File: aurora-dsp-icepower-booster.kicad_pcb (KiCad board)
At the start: 2 copper layers, 0 parts

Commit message: chore: 🔄 update code structure for better maintainability
* Refactored multiple code sections to improve readability.
* Removed redundant code blocks to streamline functionality.
* Enhanced modularity for easier future updates.
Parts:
- added MH1: MountingHole_3.2mm, , F.Cu at (5.00, 5.00)
- added MH1: MountingHole, MountingHole:MountingHole_3.2mm_M3_Pad, F.Cu at (5.00, 5.00)
- added MH2: MountingHole, MountingHole:MountingHole_3.2mm_M3_Pad, F.Cu at (195.0, 5.00)
- added MH3: MountingHole, MountingHole:MountingHole_3.2mm_M3_Pad, F.Cu at (5.00, 165.0)
- added MH4: MountingHole, MountingHole:MountingHole_3.2mm_M3_Pad, F.Cu at (195.0, 165.0)
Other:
- board outline added: 200 x 170 mm

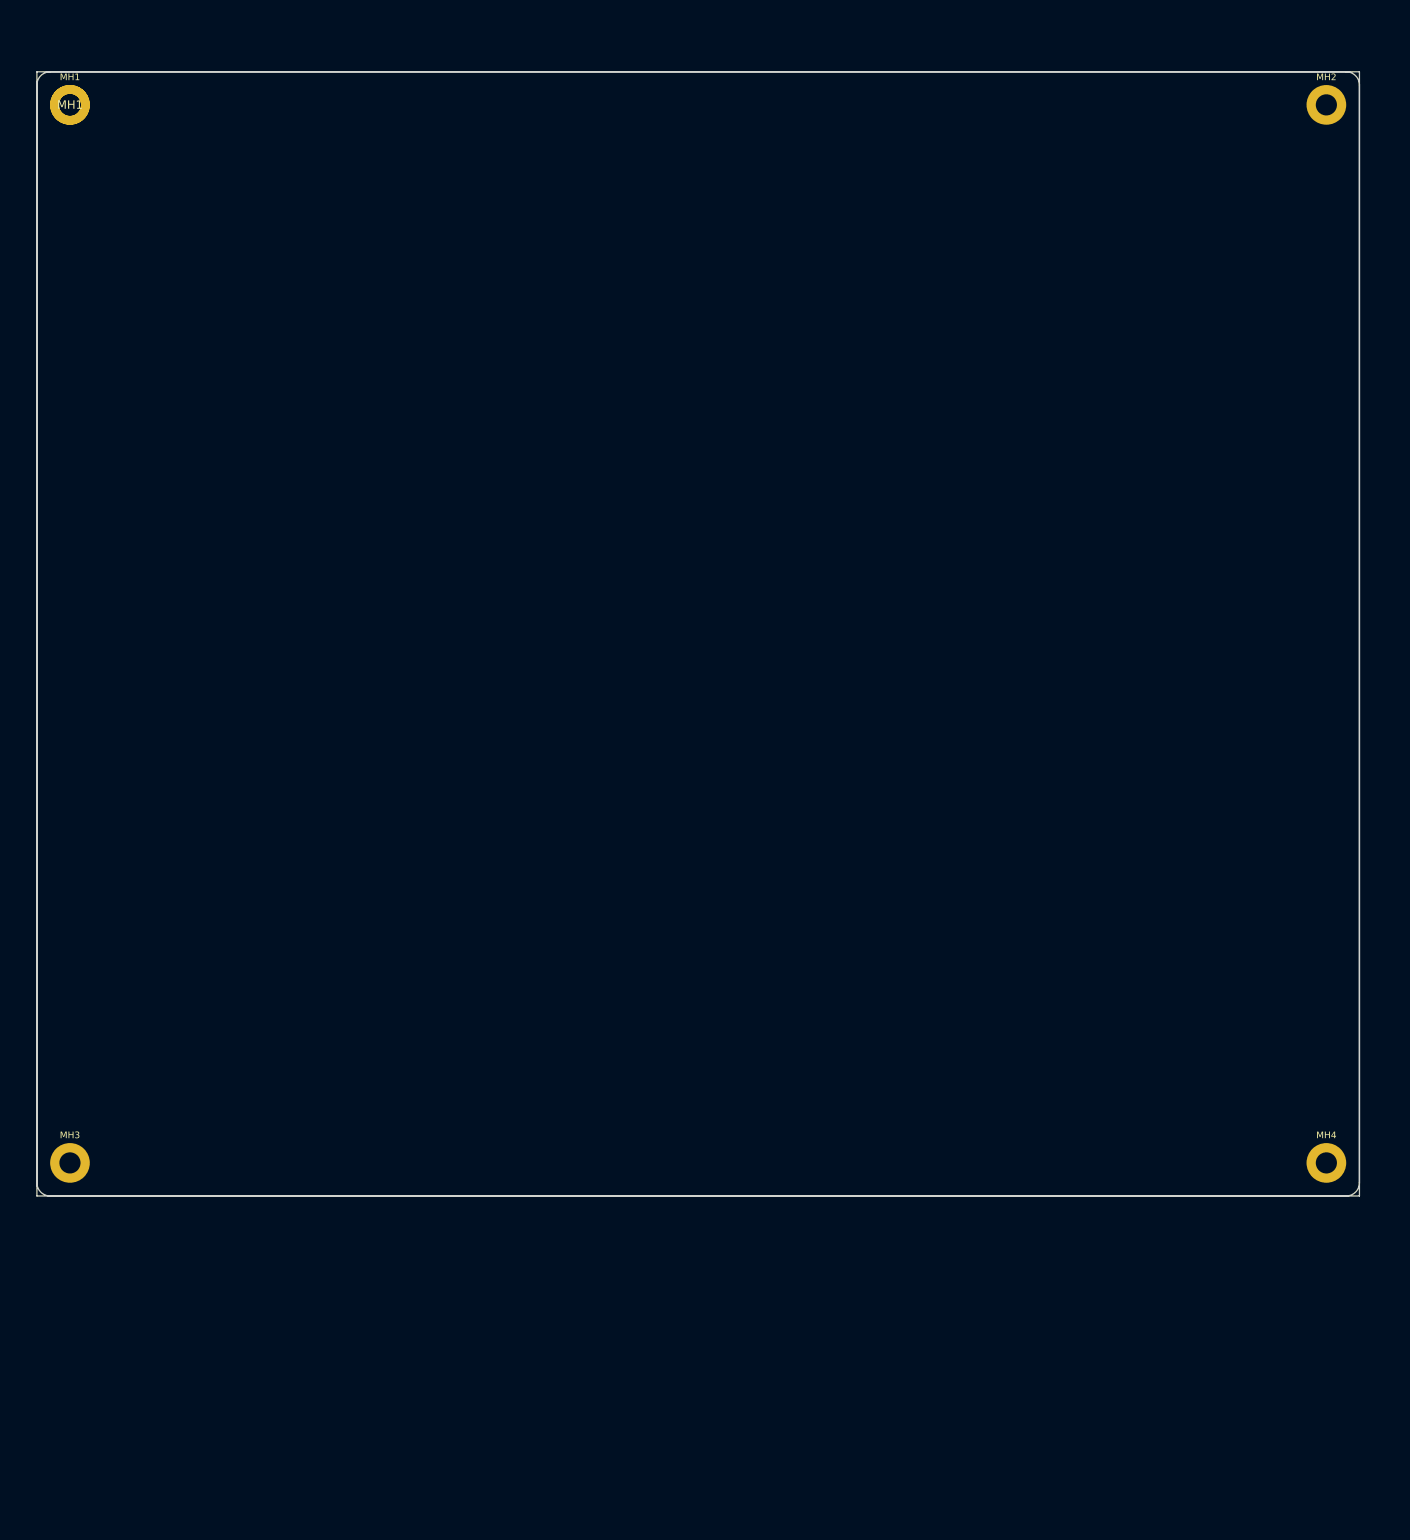
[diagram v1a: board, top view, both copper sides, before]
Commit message: feat: PCB layout v8 — routing 67%, cleanup & documentation
Schematic: 264 symbols, 0 ERC errors, all annotated
PCB: 243 footprints, 200x200mm 2-layer, v8 routing (271/400, 67%)
- Phase 0-3 complete (sync, board setup, placement)
- Phase 4 routing v8: A* pathfinding, 144 GND vias, GND zone B.Cu
- DRC: 269 violations (18 shorts, WIP), 399 unconnected (WIP)

Added:
- .gitignore for KiCad project
- FINDINGS.md: quality gate & circuit analysis
- datasheets/: ICEpower module datasheets, research docs
- scripts/pcb/: placement, netclass, mounting hole scripts
- scripts/reformat_sch.py, replicate_channels.py
- .github/skills/kicad-schematic/: references & validation scripts

Cleanup:
- Removed 13 .bak files, backups/ directory
- Removed 219 temp scripts from /tmp
- Updated .gitignore to cover *.bak*, ERC/DRC JSON, OS files
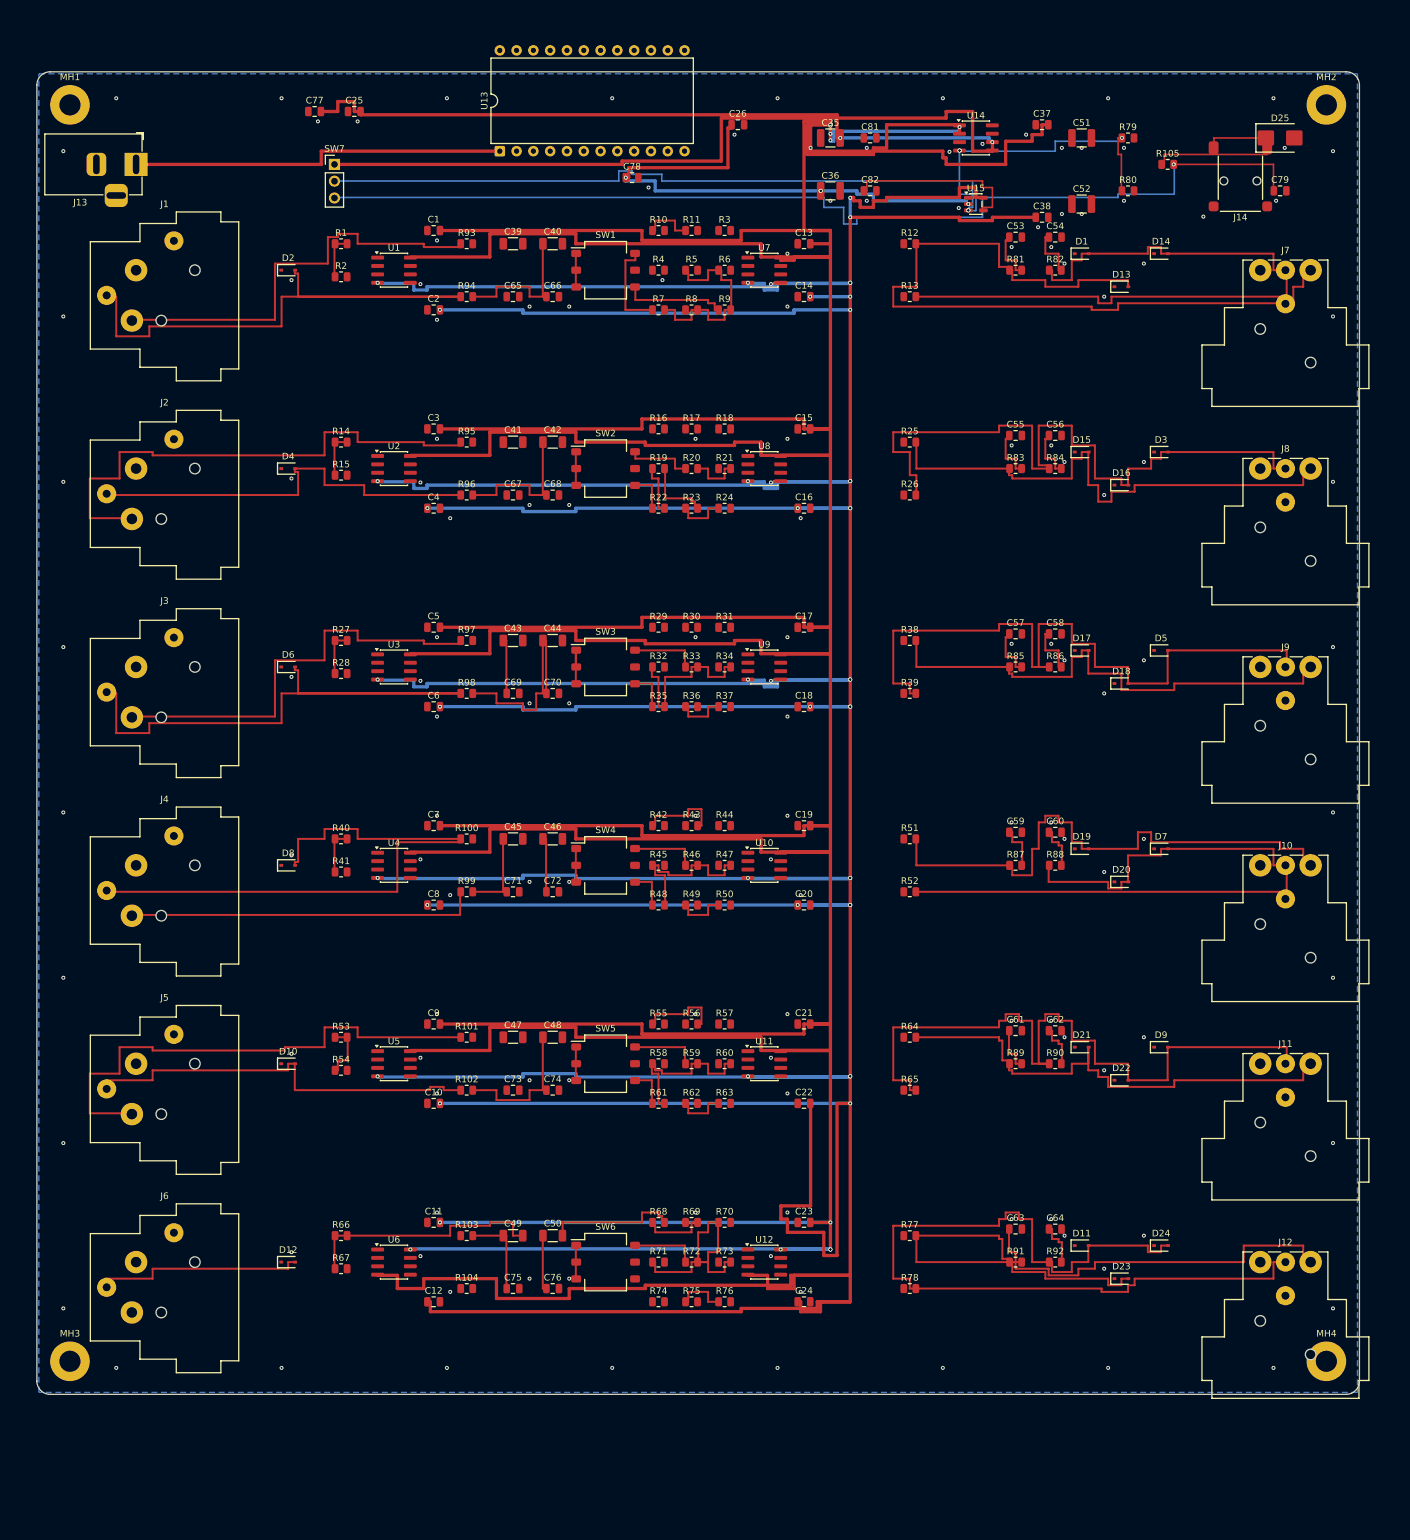
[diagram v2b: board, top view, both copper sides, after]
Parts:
- removed the MH1 at (5.00, 5.00)
- added C1: 100nF C0G, Capacitor_SMD:C_0805_2012Metric, F.Cu at (60.0, 24.0)
- added C10: 100nF C0G, Capacitor_SMD:C_0805_2012Metric, F.Cu at (60.0, 156.0)
- added C11: 100nF C0G, Capacitor_SMD:C_0805_2012Metric, F.Cu at (60.0, 174.0)
- added C12: 100nF C0G, Capacitor_SMD:C_0805_2012Metric, F.Cu at (60.0, 186.0)
- added C13: 100nF C0G, Capacitor_SMD:C_0805_2012Metric, F.Cu at (116.0, 26.0)
- added C14: 100nF C0G, Capacitor_SMD:C_0805_2012Metric, F.Cu at (116.0, 34.0)
- added C15: 100nF C0G, Capacitor_SMD:C_0805_2012Metric, F.Cu at (116.0, 54.0)
- added C16: 100nF C0G, Capacitor_SMD:C_0805_2012Metric, F.Cu at (116.0, 66.0)
- added C17: 100nF C0G, Capacitor_SMD:C_0805_2012Metric, F.Cu at (116.0, 84.0)
- added C18: 100nF C0G, Capacitor_SMD:C_0805_2012Metric, F.Cu at (116.0, 96.0)
- added C19: 100nF C0G, Capacitor_SMD:C_0805_2012Metric, F.Cu at (116.0, 114.0)
- added C2: 100nF C0G, Capacitor_SMD:C_0805_2012Metric, F.Cu at (60.0, 36.0)
- added C20: 100nF C0G, Capacitor_SMD:C_0805_2012Metric, F.Cu at (116.0, 126.0)
- added C21: 100nF C0G, Capacitor_SMD:C_0805_2012Metric, F.Cu at (116.0, 144.0)
- added C22: 100nF C0G, Capacitor_SMD:C_0805_2012Metric, F.Cu at (116.0, 156.0)
- added C23: 100nF C0G, Capacitor_SMD:C_0805_2012Metric, F.Cu at (116.0, 174.0)
- added C24: 100nF C0G, Capacitor_SMD:C_0805_2012Metric, F.Cu at (116.0, 186.0)
- added C25: 100nF C0G, Capacitor_SMD:C_0805_2012Metric, F.Cu at (48.0, 6.00)
- added C26: 100nF C0G, Capacitor_SMD:C_0805_2012Metric, F.Cu at (106.0, 8.00)
- added C3: 100nF C0G, Capacitor_SMD:C_0805_2012Metric, F.Cu at (60.0, 54.0)
- added C35: 100uF/25V, Capacitor_SMD:C_1210_3225Metric, F.Cu at (120.0, 10.0)
- added C36: 100uF/25V, Capacitor_SMD:C_1210_3225Metric, F.Cu at (120.0, 18.0)
- added C37: 10uF X5R, Capacitor_SMD:C_0805_2012Metric, F.Cu at (152.0, 8.00)
- added C38: 10uF X5R, Capacitor_SMD:C_0805_2012Metric, F.Cu at (152.0, 22.0)
- added C39: 2.2uF C0G, Capacitor_SMD:C_1206_3216Metric, F.Cu at (72.0, 26.0)
- added C4: 100nF C0G, Capacitor_SMD:C_0805_2012Metric, F.Cu at (60.0, 66.0)
- added C40: 2.2uF C0G, Capacitor_SMD:C_1206_3216Metric, F.Cu at (78.0, 26.0)
- added C41: 2.2uF C0G, Capacitor_SMD:C_1206_3216Metric, F.Cu at (72.0, 56.0)
- added C42: 2.2uF C0G, Capacitor_SMD:C_1206_3216Metric, F.Cu at (78.0, 56.0)
- added C43: 2.2uF C0G, Capacitor_SMD:C_1206_3216Metric, F.Cu at (72.0, 86.0)
- added C44: 2.2uF C0G, Capacitor_SMD:C_1206_3216Metric, F.Cu at (78.0, 86.0)
- added C45: 2.2uF C0G, Capacitor_SMD:C_1206_3216Metric, F.Cu at (72.0, 116.0)
- added C46: 2.2uF C0G, Capacitor_SMD:C_1206_3216Metric, F.Cu at (78.0, 116.0)
- added C47: 2.2uF C0G, Capacitor_SMD:C_1206_3216Metric, F.Cu at (72.0, 146.0)
- added C48: 2.2uF C0G, Capacitor_SMD:C_1206_3216Metric, F.Cu at (78.0, 146.0)
- added C49: 2.2uF C0G, Capacitor_SMD:C_1206_3216Metric, F.Cu at (72.0, 176.0)
- added C5: 100nF C0G, Capacitor_SMD:C_0805_2012Metric, F.Cu at (60.0, 84.0)
- added C50: 2.2uF C0G, Capacitor_SMD:C_1206_3216Metric, F.Cu at (78.0, 176.0)
- added C51: 100uF, Capacitor_SMD:C_1210_3225Metric, F.Cu at (158.0, 10.0)
- added C52: 100uF, Capacitor_SMD:C_1210_3225Metric, F.Cu at (158.0, 20.0)
- added C53: 100nF C0G, Capacitor_SMD:C_0805_2012Metric, F.Cu at (148.0, 25.0)
- added C54: 100nF C0G, Capacitor_SMD:C_0805_2012Metric, F.Cu at (154.0, 25.0)
- added C55: 100nF C0G, Capacitor_SMD:C_0805_2012Metric, F.Cu at (148.0, 55.0)
- added C56: 100nF C0G, Capacitor_SMD:C_0805_2012Metric, F.Cu at (154.0, 55.0)
- added C57: 100nF C0G, Capacitor_SMD:C_0805_2012Metric, F.Cu at (148.0, 85.0)
- added C58: 100nF C0G, Capacitor_SMD:C_0805_2012Metric, F.Cu at (154.0, 85.0)
- added C59: 100nF C0G, Capacitor_SMD:C_0805_2012Metric, F.Cu at (148.0, 115.0)
- added C6: 100nF C0G, Capacitor_SMD:C_0805_2012Metric, F.Cu at (60.0, 96.0)
- added C60: 100nF C0G, Capacitor_SMD:C_0805_2012Metric, F.Cu at (154.0, 115.0)
- added C61: 100nF C0G, Capacitor_SMD:C_0805_2012Metric, F.Cu at (148.0, 145.0)
- added C62: 100nF C0G, Capacitor_SMD:C_0805_2012Metric, F.Cu at (154.0, 145.0)
- added C63: 100nF C0G, Capacitor_SMD:C_0805_2012Metric, F.Cu at (148.0, 175.0)
- added C64: 100nF C0G, Capacitor_SMD:C_0805_2012Metric, F.Cu at (154.0, 175.0)
- added C65: 100pF C0G, Capacitor_SMD:C_0805_2012Metric, F.Cu at (72.0, 34.0)
- added C66: 100pF C0G, Capacitor_SMD:C_0805_2012Metric, F.Cu at (78.0, 34.0)
- added C67: 100pF C0G, Capacitor_SMD:C_0805_2012Metric, F.Cu at (72.0, 64.0)
- added C68: 100pF C0G, Capacitor_SMD:C_0805_2012Metric, F.Cu at (78.0, 64.0)
- added C69: 100pF C0G, Capacitor_SMD:C_0805_2012Metric, F.Cu at (72.0, 94.0)
- added C7: 100nF C0G, Capacitor_SMD:C_0805_2012Metric, F.Cu at (60.0, 114.0)
- added C70: 100pF C0G, Capacitor_SMD:C_0805_2012Metric, F.Cu at (78.0, 94.0)
- added C71: 100pF C0G, Capacitor_SMD:C_0805_2012Metric, F.Cu at (72.0, 124.0)
- added C72: 100pF C0G, Capacitor_SMD:C_0805_2012Metric, F.Cu at (78.0, 124.0)
- added C73: 100pF C0G, Capacitor_SMD:C_0805_2012Metric, F.Cu at (72.0, 154.0)
- added C74: 100pF C0G, Capacitor_SMD:C_0805_2012Metric, F.Cu at (78.0, 154.0)
- added C75: 100pF C0G, Capacitor_SMD:C_0805_2012Metric, F.Cu at (72.0, 184.0)
- added C76: 100pF C0G, Capacitor_SMD:C_0805_2012Metric, F.Cu at (78.0, 184.0)
- added C77: 100nF C0G, Capacitor_SMD:C_0805_2012Metric, F.Cu at (42.0, 6.00)
- added C78: 100nF C0G, Capacitor_SMD:C_0805_2012Metric, F.Cu at (90.0, 16.0)
- added C79: 100nF C0G, Capacitor_SMD:C_0805_2012Metric, F.Cu at (188.0, 18.0)
- added C8: 100nF C0G, Capacitor_SMD:C_0805_2012Metric, F.Cu at (60.0, 126.0)
- added C81: 100nF C0G, Capacitor_SMD:C_0805_2012Metric, F.Cu at (126.0, 10.0)
- added C82: 100nF C0G, Capacitor_SMD:C_0805_2012Metric, F.Cu at (126.0, 18.0)
- added C9: 100nF C0G, Capacitor_SMD:C_0805_2012Metric, F.Cu at (60.0, 144.0)
- added D1: PESD5V0S1BL, Diode_SMD:D_SOD-323, F.Cu at (158.0, 27.5)
- added D10: PESD5V0S1BL, Diode_SMD:D_SOD-323, F.Cu at (38.0, 150.0)
- added D11: PESD5V0S1BL, Diode_SMD:D_SOD-323, F.Cu at (158.0, 177.5)
- added D12: PESD5V0S1BL, Diode_SMD:D_SOD-323, F.Cu at (38.0, 180.0)
- added D13: PESD5V0S1BL, Diode_SMD:D_SOD-323, F.Cu at (164.0, 32.5)
- added D14: PESD5V0S1BL, Diode_SMD:D_SOD-323, F.Cu at (170.0, 27.5)
- added D15: PESD5V0S1BL, Diode_SMD:D_SOD-323, F.Cu at (158.0, 57.5)
- added D16: PESD5V0S1BL, Diode_SMD:D_SOD-323, F.Cu at (164.0, 62.5)
- added D17: PESD5V0S1BL, Diode_SMD:D_SOD-323, F.Cu at (158.0, 87.5)
- added D18: PESD5V0S1BL, Diode_SMD:D_SOD-323, F.Cu at (164.0, 92.5)
- added D19: PESD5V0S1BL, Diode_SMD:D_SOD-323, F.Cu at (158.0, 117.5)
- added D2: PESD5V0S1BL, Diode_SMD:D_SOD-323, F.Cu at (38.0, 30.0)
- added D20: PESD5V0S1BL, Diode_SMD:D_SOD-323, F.Cu at (164.0, 122.5)
- added D21: PESD5V0S1BL, Diode_SMD:D_SOD-323, F.Cu at (158.0, 147.5)
- added D22: PESD5V0S1BL, Diode_SMD:D_SOD-323, F.Cu at (164.0, 152.5)
- added D23: PESD5V0S1BL, Diode_SMD:D_SOD-323, F.Cu at (164.0, 182.5)
- added D24: PESD5V0S1BL, Diode_SMD:D_SOD-323, F.Cu at (170.0, 177.5)
- added D25: SMBJ15CA, Diode_SMD:D_SMB, F.Cu at (188.0, 10.0)
- added D3: PESD5V0S1BL, Diode_SMD:D_SOD-323, F.Cu at (170.0, 57.5)
- added D4: PESD5V0S1BL, Diode_SMD:D_SOD-323, F.Cu at (38.0, 60.0)
- added D5: PESD5V0S1BL, Diode_SMD:D_SOD-323, F.Cu at (170.0, 87.5)
- added D6: PESD5V0S1BL, Diode_SMD:D_SOD-323, F.Cu at (38.0, 90.0)
- added D7: PESD5V0S1BL, Diode_SMD:D_SOD-323, F.Cu at (170.0, 117.5)
- added D8: PESD5V0S1BL, Diode_SMD:D_SOD-323, F.Cu at (38.0, 120.0)
- added D9: PESD5V0S1BL, Diode_SMD:D_SOD-323, F.Cu at (170.0, 147.5)
- added J1: XLR_IN_1, Connector_Audio:Jack_XLR_Neutrik_NC3FBH2_Horizontal, F.Cu at (15.0, 30.0)
- added J10: XLR3_OUT, Connector_Audio:Jack_XLR_Neutrik_NC3MBH_Horizontal, F.Cu at (185.0, 120.0)
- added J11: XLR3_OUT, Connector_Audio:Jack_XLR_Neutrik_NC3MBH_Horizontal, F.Cu at (185.0, 150.0)
- added J12: XLR3_OUT, Connector_Audio:Jack_XLR_Neutrik_NC3MBH_Horizontal, F.Cu at (185.0, 180.0)
- added J13: 24V DC, Connector_BarrelJack:BarrelJack_Horizontal, F.Cu at (15.0, 14.0)
- added J14: REMOTE 3.5mm, Connector_Audio:Jack_3.5mm_Lumberg_1503_02_Horizontal, F.Cu at (182.0, 14.0)
- added J2: XLR_IN_2, Connector_Audio:Jack_XLR_Neutrik_NC3FBH2_Horizontal, F.Cu at (15.0, 60.0)
- added J3: XLR_IN_3, Connector_Audio:Jack_XLR_Neutrik_NC3FBH2_Horizontal, F.Cu at (15.0, 90.0)
- added J4: XLR_IN_4, Connector_Audio:Jack_XLR_Neutrik_NC3FBH2_Horizontal, F.Cu at (15.0, 120.0)
- added J5: XLR_IN_5, Connector_Audio:Jack_XLR_Neutrik_NC3FBH2_Horizontal, F.Cu at (15.0, 150.0)
- added J6: XLR_IN_6, Connector_Audio:Jack_XLR_Neutrik_NC3FBH2_Horizontal, F.Cu at (15.0, 180.0)
- added J7: XLR3_OUT, Connector_Audio:Jack_XLR_Neutrik_NC3MBH_Horizontal, F.Cu at (185.0, 30.0)
- added J8: XLR3_OUT, Connector_Audio:Jack_XLR_Neutrik_NC3MBH_Horizontal, F.Cu at (185.0, 60.0)
- added J9: XLR3_OUT, Connector_Audio:Jack_XLR_Neutrik_NC3MBH_Horizontal, F.Cu at (185.0, 90.0)
- added R1: 10k 0.1%, Resistor_SMD:R_0805_2012Metric, F.Cu at (46.0, 26.0)
- added R10: 10k, Resistor_SMD:R_0805_2012Metric, F.Cu at (94.0, 24.0)
- added R100: 47, Resistor_SMD:R_0805_2012Metric, F.Cu at (65.0, 116.0)
- added R101: 47, Resistor_SMD:R_0805_2012Metric, F.Cu at (65.0, 146.0)
- added R102: 47, Resistor_SMD:R_0805_2012Metric, F.Cu at (65.0, 154.0)
- added R103: 47, Resistor_SMD:R_0805_2012Metric, F.Cu at (65.0, 176.0)
- added R104: 47, Resistor_SMD:R_0805_2012Metric, F.Cu at (65.0, 184.0)
- added R105: 10k, Resistor_SMD:R_0805_2012Metric, F.Cu at (171.0, 14.0)
- added R11: 10k, Resistor_SMD:R_0805_2012Metric, F.Cu at (99.0, 24.0)
- added R12: 47, Resistor_SMD:R_0805_2012Metric, F.Cu at (132.0, 26.0)
- added R13: 47, Resistor_SMD:R_0805_2012Metric, F.Cu at (132.0, 34.0)
- added R14: 10k 0.1%, Resistor_SMD:R_0805_2012Metric, F.Cu at (46.0, 56.0)
- added R15: 10k 0.1%, Resistor_SMD:R_0805_2012Metric, F.Cu at (46.0, 61.0)
- added R16: 10k 0.1%, Resistor_SMD:R_0805_2012Metric, F.Cu at (94.0, 54.0)
- added R17: 10k 0.1%, Resistor_SMD:R_0805_2012Metric, F.Cu at (99.0, 54.0)
- added R18: 10k 0.1%, Resistor_SMD:R_0805_2012Metric, F.Cu at (104.0, 54.0)
- added R19: 10k 0.1%, Resistor_SMD:R_0805_2012Metric, F.Cu at (94.0, 60.0)
- added R2: 10k 0.1%, Resistor_SMD:R_0805_2012Metric, F.Cu at (46.0, 31.0)
- added R20: 30k, Resistor_SMD:R_0805_2012Metric, F.Cu at (99.0, 60.0)
- added R21: 15k, Resistor_SMD:R_0805_2012Metric, F.Cu at (104.0, 60.0)
- added R22: 7.5k, Resistor_SMD:R_0805_2012Metric, F.Cu at (94.0, 66.0)
- added R23: 10k, Resistor_SMD:R_0805_2012Metric, F.Cu at (99.0, 66.0)
- added R24: 10k, Resistor_SMD:R_0805_2012Metric, F.Cu at (104.0, 66.0)
- added R25: 47, Resistor_SMD:R_0805_2012Metric, F.Cu at (132.0, 56.0)
- added R26: 47, Resistor_SMD:R_0805_2012Metric, F.Cu at (132.0, 64.0)
- added R27: 10k 0.1%, Resistor_SMD:R_0805_2012Metric, F.Cu at (46.0, 86.0)
- added R28: 10k 0.1%, Resistor_SMD:R_0805_2012Metric, F.Cu at (46.0, 91.0)
- added R29: 10k 0.1%, Resistor_SMD:R_0805_2012Metric, F.Cu at (94.0, 84.0)
- added R3: 10k 0.1%, Resistor_SMD:R_0805_2012Metric, F.Cu at (104.0, 24.0)
- added R30: 10k 0.1%, Resistor_SMD:R_0805_2012Metric, F.Cu at (99.0, 84.0)
- added R31: 10k 0.1%, Resistor_SMD:R_0805_2012Metric, F.Cu at (104.0, 84.0)
- added R32: 10k 0.1%, Resistor_SMD:R_0805_2012Metric, F.Cu at (94.0, 90.0)
- added R33: 30k, Resistor_SMD:R_0805_2012Metric, F.Cu at (99.0, 90.0)
- added R34: 15k, Resistor_SMD:R_0805_2012Metric, F.Cu at (104.0, 90.0)
- added R35: 7.5k, Resistor_SMD:R_0805_2012Metric, F.Cu at (94.0, 96.0)
- added R36: 10k, Resistor_SMD:R_0805_2012Metric, F.Cu at (99.0, 96.0)
- added R37: 10k, Resistor_SMD:R_0805_2012Metric, F.Cu at (104.0, 96.0)
- added R38: 47, Resistor_SMD:R_0805_2012Metric, F.Cu at (132.0, 86.0)
- added R39: 47, Resistor_SMD:R_0805_2012Metric, F.Cu at (132.0, 94.0)
- added R4: 10k 0.1%, Resistor_SMD:R_0805_2012Metric, F.Cu at (94.0, 30.0)
- added R40: 10k 0.1%, Resistor_SMD:R_0805_2012Metric, F.Cu at (46.0, 116.0)
- added R41: 10k 0.1%, Resistor_SMD:R_0805_2012Metric, F.Cu at (46.0, 121.0)
- added R42: 10k 0.1%, Resistor_SMD:R_0805_2012Metric, F.Cu at (94.0, 114.0)
- added R43: 10k 0.1%, Resistor_SMD:R_0805_2012Metric, F.Cu at (99.0, 114.0)
- added R44: 10k 0.1%, Resistor_SMD:R_0805_2012Metric, F.Cu at (104.0, 114.0)
- added R45: 10k 0.1%, Resistor_SMD:R_0805_2012Metric, F.Cu at (94.0, 120.0)
- added R46: 30k, Resistor_SMD:R_0805_2012Metric, F.Cu at (99.0, 120.0)
- added R47: 15k, Resistor_SMD:R_0805_2012Metric, F.Cu at (104.0, 120.0)
- added R48: 7.5k, Resistor_SMD:R_0805_2012Metric, F.Cu at (94.0, 126.0)
- added R49: 10k, Resistor_SMD:R_0805_2012Metric, F.Cu at (99.0, 126.0)
- added R5: 10k 0.1%, Resistor_SMD:R_0805_2012Metric, F.Cu at (99.0, 30.0)
- added R50: 10k, Resistor_SMD:R_0805_2012Metric, F.Cu at (104.0, 126.0)
- added R51: 47, Resistor_SMD:R_0805_2012Metric, F.Cu at (132.0, 116.0)
- added R52: 47, Resistor_SMD:R_0805_2012Metric, F.Cu at (132.0, 124.0)
- added R53: 10k 0.1%, Resistor_SMD:R_0805_2012Metric, F.Cu at (46.0, 146.0)
- added R54: 10k 0.1%, Resistor_SMD:R_0805_2012Metric, F.Cu at (46.0, 151.0)
- added R55: 10k 0.1%, Resistor_SMD:R_0805_2012Metric, F.Cu at (94.0, 144.0)
- added R56: 10k 0.1%, Resistor_SMD:R_0805_2012Metric, F.Cu at (99.0, 144.0)
- added R57: 10k 0.1%, Resistor_SMD:R_0805_2012Metric, F.Cu at (104.0, 144.0)
- added R58: 10k 0.1%, Resistor_SMD:R_0805_2012Metric, F.Cu at (94.0, 150.0)
- added R59: 30k, Resistor_SMD:R_0805_2012Metric, F.Cu at (99.0, 150.0)
- added R6: 10k 0.1%, Resistor_SMD:R_0805_2012Metric, F.Cu at (104.0, 30.0)
- added R60: 15k, Resistor_SMD:R_0805_2012Metric, F.Cu at (104.0, 150.0)
- added R61: 7.5k, Resistor_SMD:R_0805_2012Metric, F.Cu at (94.0, 156.0)
- added R62: 10k, Resistor_SMD:R_0805_2012Metric, F.Cu at (99.0, 156.0)
- added R63: 10k, Resistor_SMD:R_0805_2012Metric, F.Cu at (104.0, 156.0)
- added R64: 47, Resistor_SMD:R_0805_2012Metric, F.Cu at (132.0, 146.0)
- added R65: 47, Resistor_SMD:R_0805_2012Metric, F.Cu at (132.0, 154.0)
- added R66: 10k 0.1%, Resistor_SMD:R_0805_2012Metric, F.Cu at (46.0, 176.0)
- added R67: 10k 0.1%, Resistor_SMD:R_0805_2012Metric, F.Cu at (46.0, 181.0)
- added R68: 10k 0.1%, Resistor_SMD:R_0805_2012Metric, F.Cu at (94.0, 174.0)
- added R69: 10k 0.1%, Resistor_SMD:R_0805_2012Metric, F.Cu at (99.0, 174.0)
- added R7: 30k, Resistor_SMD:R_0805_2012Metric, F.Cu at (94.0, 36.0)
- added R70: 10k 0.1%, Resistor_SMD:R_0805_2012Metric, F.Cu at (104.0, 174.0)
- added R71: 10k 0.1%, Resistor_SMD:R_0805_2012Metric, F.Cu at (94.0, 180.0)
- added R72: 30k, Resistor_SMD:R_0805_2012Metric, F.Cu at (99.0, 180.0)
- added R73: 15k, Resistor_SMD:R_0805_2012Metric, F.Cu at (104.0, 180.0)
- added R74: 7.5k, Resistor_SMD:R_0805_2012Metric, F.Cu at (94.0, 186.0)
- added R75: 10k, Resistor_SMD:R_0805_2012Metric, F.Cu at (99.0, 186.0)
- added R76: 10k, Resistor_SMD:R_0805_2012Metric, F.Cu at (104.0, 186.0)
- added R77: 47, Resistor_SMD:R_0805_2012Metric, F.Cu at (132.0, 176.0)
- added R78: 47, Resistor_SMD:R_0805_2012Metric, F.Cu at (132.0, 184.0)
- added R79: 100k, Resistor_SMD:R_0805_2012Metric, F.Cu at (165.0, 10.0)
- added R8: 15k, Resistor_SMD:R_0805_2012Metric, F.Cu at (99.0, 36.0)
- added R80: 100k, Resistor_SMD:R_0805_2012Metric, F.Cu at (165.0, 18.0)
- added R81: 10, Resistor_SMD:R_0805_2012Metric, F.Cu at (148.0, 30.0)
- added R82: 10, Resistor_SMD:R_0805_2012Metric, F.Cu at (154.0, 30.0)
- added R83: 10, Resistor_SMD:R_0805_2012Metric, F.Cu at (148.0, 60.0)
- added R84: 10, Resistor_SMD:R_0805_2012Metric, F.Cu at (154.0, 60.0)
- added R85: 10, Resistor_SMD:R_0805_2012Metric, F.Cu at (148.0, 90.0)
- added R86: 10, Resistor_SMD:R_0805_2012Metric, F.Cu at (154.0, 90.0)
- added R87: 10, Resistor_SMD:R_0805_2012Metric, F.Cu at (148.0, 120.0)
- added R88: 10, Resistor_SMD:R_0805_2012Metric, F.Cu at (154.0, 120.0)
- added R89: 10, Resistor_SMD:R_0805_2012Metric, F.Cu at (148.0, 150.0)
- added R9: 7.5k, Resistor_SMD:R_0805_2012Metric, F.Cu at (104.0, 36.0)
- added R90: 10, Resistor_SMD:R_0805_2012Metric, F.Cu at (154.0, 150.0)
- added R91: 10, Resistor_SMD:R_0805_2012Metric, F.Cu at (148.0, 180.0)
- added R92: 10, Resistor_SMD:R_0805_2012Metric, F.Cu at (154.0, 180.0)
- added R93: 47, Resistor_SMD:R_0805_2012Metric, F.Cu at (65.0, 26.0)
- added R94: 47, Resistor_SMD:R_0805_2012Metric, F.Cu at (65.0, 34.0)
- added R95: 47, Resistor_SMD:R_0805_2012Metric, F.Cu at (65.0, 56.0)
- added R96: 47, Resistor_SMD:R_0805_2012Metric, F.Cu at (65.0, 64.0)
- added R97: 47, Resistor_SMD:R_0805_2012Metric, F.Cu at (65.0, 86.0)
- added R98: 47, Resistor_SMD:R_0805_2012Metric, F.Cu at (65.0, 94.0)
- added R99: 47, Resistor_SMD:R_0805_2012Metric, F.Cu at (65.0, 124.0)
- added SW1: Gain CH1, Button_Switch_SMD:SW_DIP_SPSTx03_Slide_Omron_A6S-310x_W8.9mm_P2.54mm, F.Cu at (86.0, 30.0)
- added SW2: Gain CH2, Button_Switch_SMD:SW_DIP_SPSTx03_Slide_Omron_A6S-310x_W8.9mm_P2.54mm, F.Cu at (86.0, 60.0)
- added SW3: Gain CH3, Button_Switch_SMD:SW_DIP_SPSTx03_Slide_Omron_A6S-310x_W8.9mm_P2.54mm, F.Cu at (86.0, 90.0)
- added SW4: Gain CH4, Button_Switch_SMD:SW_DIP_SPSTx03_Slide_Omron_A6S-310x_W8.9mm_P2.54mm, F.Cu at (86.0, 120.0)
- added SW5: Gain CH5, Button_Switch_SMD:SW_DIP_SPSTx03_Slide_Omron_A6S-310x_W8.9mm_P2.54mm, F.Cu at (86.0, 150.0)
- added SW6: Gain CH6, Button_Switch_SMD:SW_DIP_SPSTx03_Slide_Omron_A6S-310x_W8.9mm_P2.54mm, F.Cu at (86.0, 180.0)
- added SW7: ALWAYS/REMOTE, Connector_PinHeader_2.54mm:PinHeader_1x03_P2.54mm_Vertical, F.Cu at (45.0, 14.0)
- added U1: LM4562, Package_SO:SOIC-8_3.9x4.9mm_P1.27mm, F.Cu at (54.0, 30.0)
- added U10: LM4562, Package_SO:SOIC-8_3.9x4.9mm_P1.27mm, F.Cu at (110.0, 120.0)
- added U11: LM4562, Package_SO:SOIC-8_3.9x4.9mm_P1.27mm, F.Cu at (110.0, 150.0)
- added U12: LM4562, Package_SO:SOIC-8_3.9x4.9mm_P1.27mm, F.Cu at (110.0, 180.0)
- added U13: TEL5-2422, Package_DIP:DIP-24_W15.24mm, F.Cu at (70.0, 12.0)
- added U14: ADP7118ARDZ-11, Package_SO:SOIC-8_3.9x4.9mm_P1.27mm, F.Cu at (142.0, 10.0)
- added U15: ADP7182AUJZ-11, Package_TO_SOT_SMD:SOT-23-5, F.Cu at (142.0, 20.0)
- added U2: LM4562, Package_SO:SOIC-8_3.9x4.9mm_P1.27mm, F.Cu at (54.0, 60.0)
- added U3: LM4562, Package_SO:SOIC-8_3.9x4.9mm_P1.27mm, F.Cu at (54.0, 90.0)
- added U4: LM4562, Package_SO:SOIC-8_3.9x4.9mm_P1.27mm, F.Cu at (54.0, 120.0)
- added U5: LM4562, Package_SO:SOIC-8_3.9x4.9mm_P1.27mm, F.Cu at (54.0, 150.0)
- added U6: LM4562, Package_SO:SOIC-8_3.9x4.9mm_P1.27mm, F.Cu at (54.0, 180.0)
- added U7: LM4562, Package_SO:SOIC-8_3.9x4.9mm_P1.27mm, F.Cu at (110.0, 30.0)
- added U8: LM4562, Package_SO:SOIC-8_3.9x4.9mm_P1.27mm, F.Cu at (110.0, 60.0)
- added U9: LM4562, Package_SO:SOIC-8_3.9x4.9mm_P1.27mm, F.Cu at (110.0, 90.0)
- moved MH3 30.0 mm to (5.00, 195.0)
- moved MH4 30.0 mm to (195.0, 195.0)
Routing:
- net /V-: track 0.00 -> 1256.0 mm, vias 0 -> 43
- net /V+: track 0.00 -> 1143.0 mm, vias 0 -> 15
- net /+12V: track 0.00 -> 224.0 mm, vias 0 -> 2
- net /CH5_OUT_COLD: track 0.00 -> 188.0 mm
- net /CH2_OUT_COLD: track 0.00 -> 185.0 mm
- net /CH1_OUT_COLD: track 0.00 -> 173.0 mm
- net /CH3_OUT_COLD: track 0.00 -> 171.0 mm
- net /CH4_OUT_COLD: track 0.00 -> 161.0 mm
- net /REMOTE_FILT: track 0.00 -> 159.0 mm, vias 0 -> 2
- net /EN_CTRL: track 0.00 -> 152.5 mm, vias 0 -> 6
- net /CH6_OUT_COLD: track 0.00 -> 132.5 mm
- net /CH1_OUT_HOT: track 0.00 -> 123.0 mm
- net /CH6_OUT_HOT: track 0.00 -> 113.0 mm
- net /CH3_COLD_RAW: track 0.00 -> 94.5 mm
- net /CH1_COLD_RAW: track 0.00 -> 94.5 mm
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- added copper zone on B.Cu, net /GND
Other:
- board size 200 x 170 mm -> 200 x 200 mm

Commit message: feat(pcb): reposition connectors for enclosure mounting
19 components moved (15 primary + 4 secondary collision fixes).
XLR IN (J1-J6): 180 deg, protrude 3.9mm left.
XLR OUT (J7-J12): 90 deg CCW, protrude 7.8mm right.
J13 (Power): barrel up, 6mm top protrusion.
J14 (Remote): moved to top edge, 2.5mm protrusion.
U13: moved down (Y=20), fully inside board.
Secondary: SW7, C77, C78, C79 relocated to resolve collisions.
All pads verified within board (0.3mm clearance).
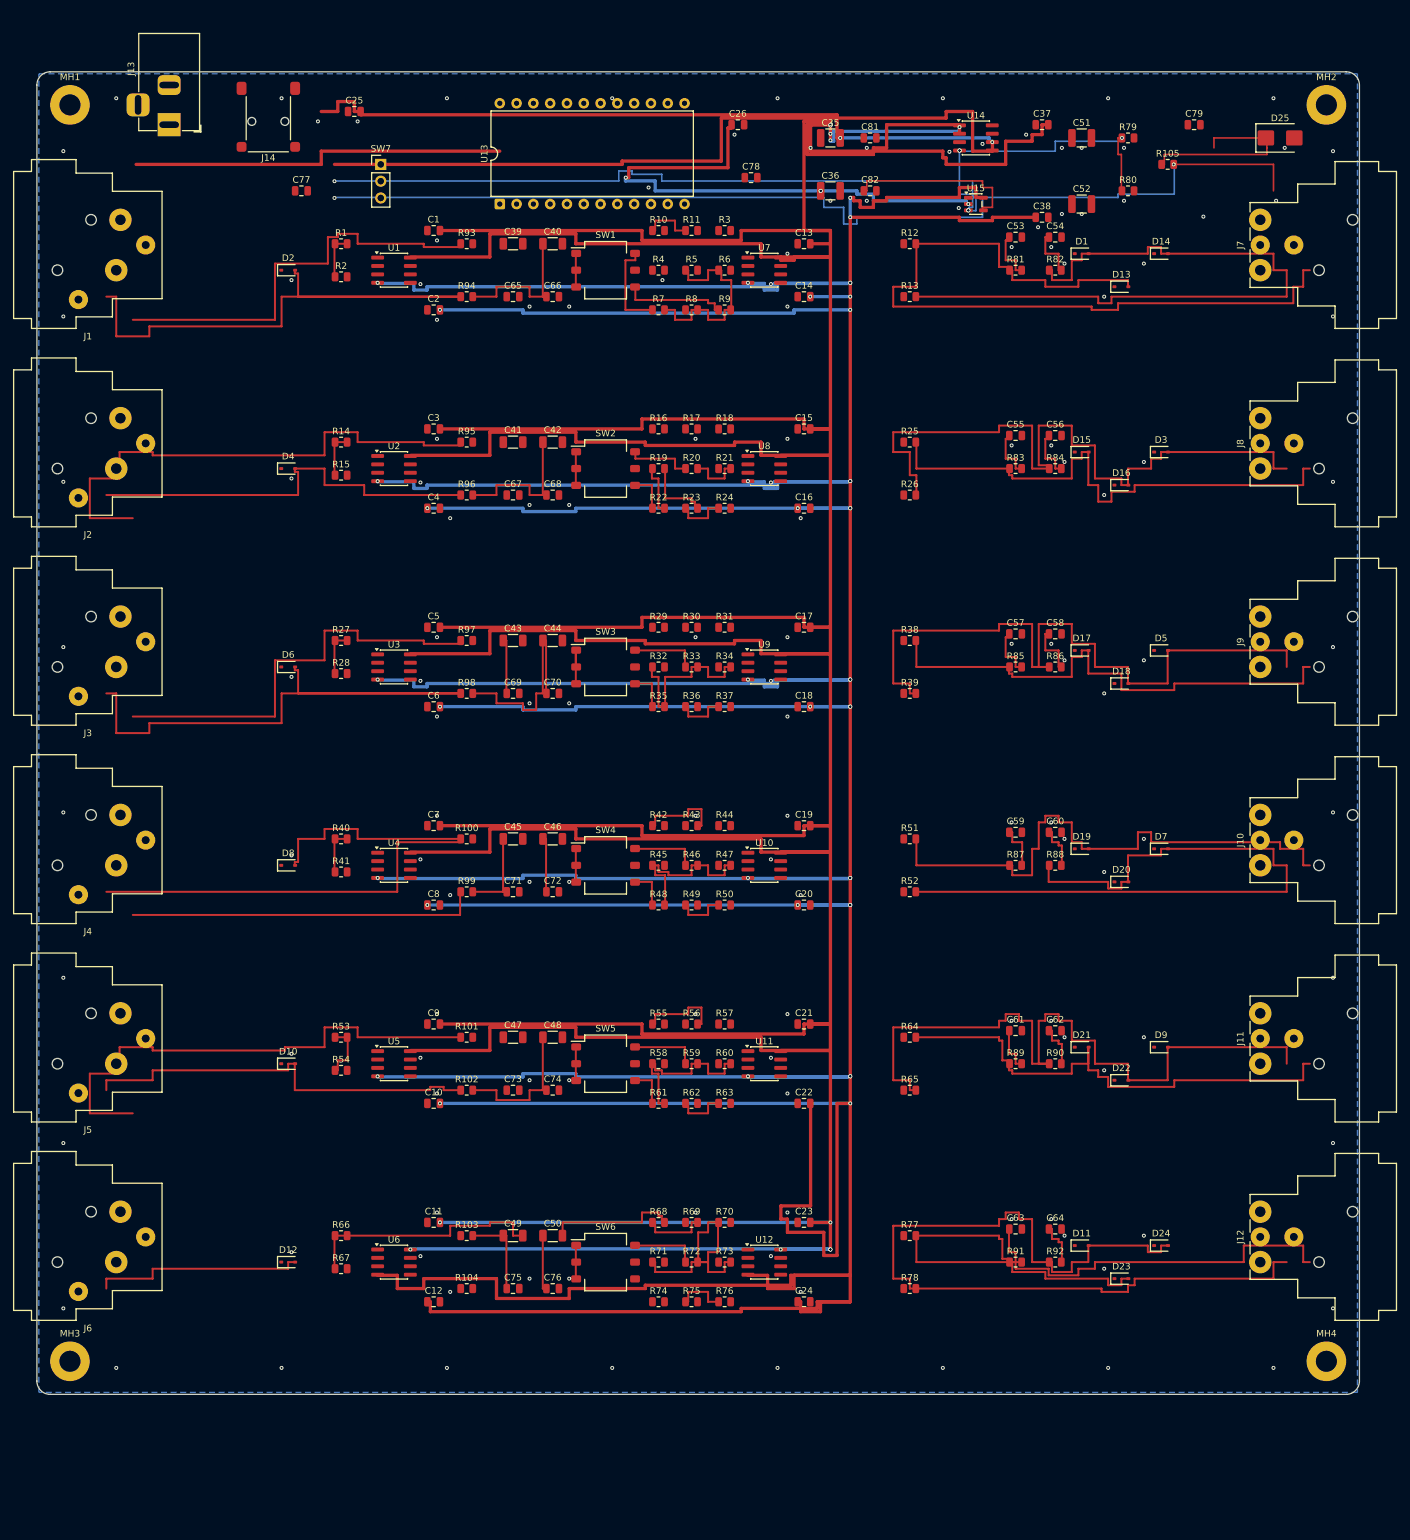
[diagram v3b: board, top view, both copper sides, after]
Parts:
- moved J14 147.3 mm to (35.0, 5.00)
- moved C78 18.0 mm to (108.0, 16.0)
- moved C79 16.4 mm to (175.0, 8.00)
- moved C77 12.2 mm to (40.0, 18.0)
- moved U13 8.00 mm to (70.0, 20.0)
- moved J13 7.81 mm to (20.0, 8.00), turned to -90 degrees
- moved SW7 7.00 mm to (52.0, 14.0)
- moved J1 3.00 mm to (12.0, 30.0), turned to 180 degrees
- moved J2 3.00 mm to (12.0, 60.0), turned to 180 degrees
- moved J3 3.00 mm to (12.0, 90.0), turned to 180 degrees
- moved J4 3.00 mm to (12.0, 120.0), turned to 180 degrees
- moved J5 3.00 mm to (12.0, 150.0), turned to 180 degrees
- moved J6 3.00 mm to (12.0, 180.0), turned to 180 degrees
- turned J10 to 90 degrees
- turned J11 to 90 degrees
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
